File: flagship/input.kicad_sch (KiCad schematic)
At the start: 13 parts, among them J1 BUS_IN, Q1 HOTSWAP_FET, Q2 IDEAL_DIODE_FET, U1 LTC4364IS-1

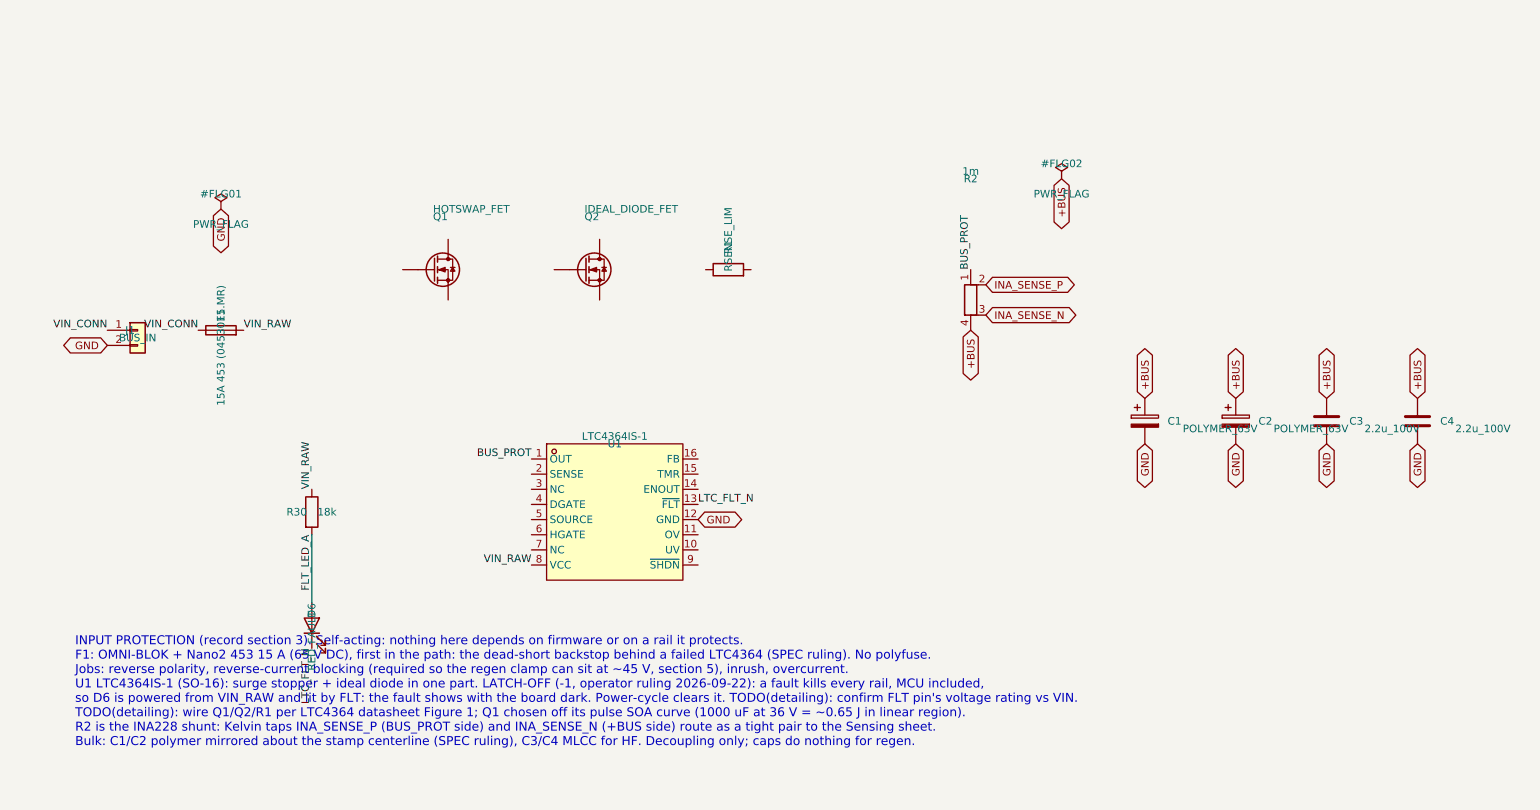
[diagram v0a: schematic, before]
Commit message: flagship: input fuse soldered (Nano2 453 15 A) instead of socketed; SPEC ruling updated
Co-Authored-By: Claude Opus 5.5 (1M context) <noreply@anthropic.com>
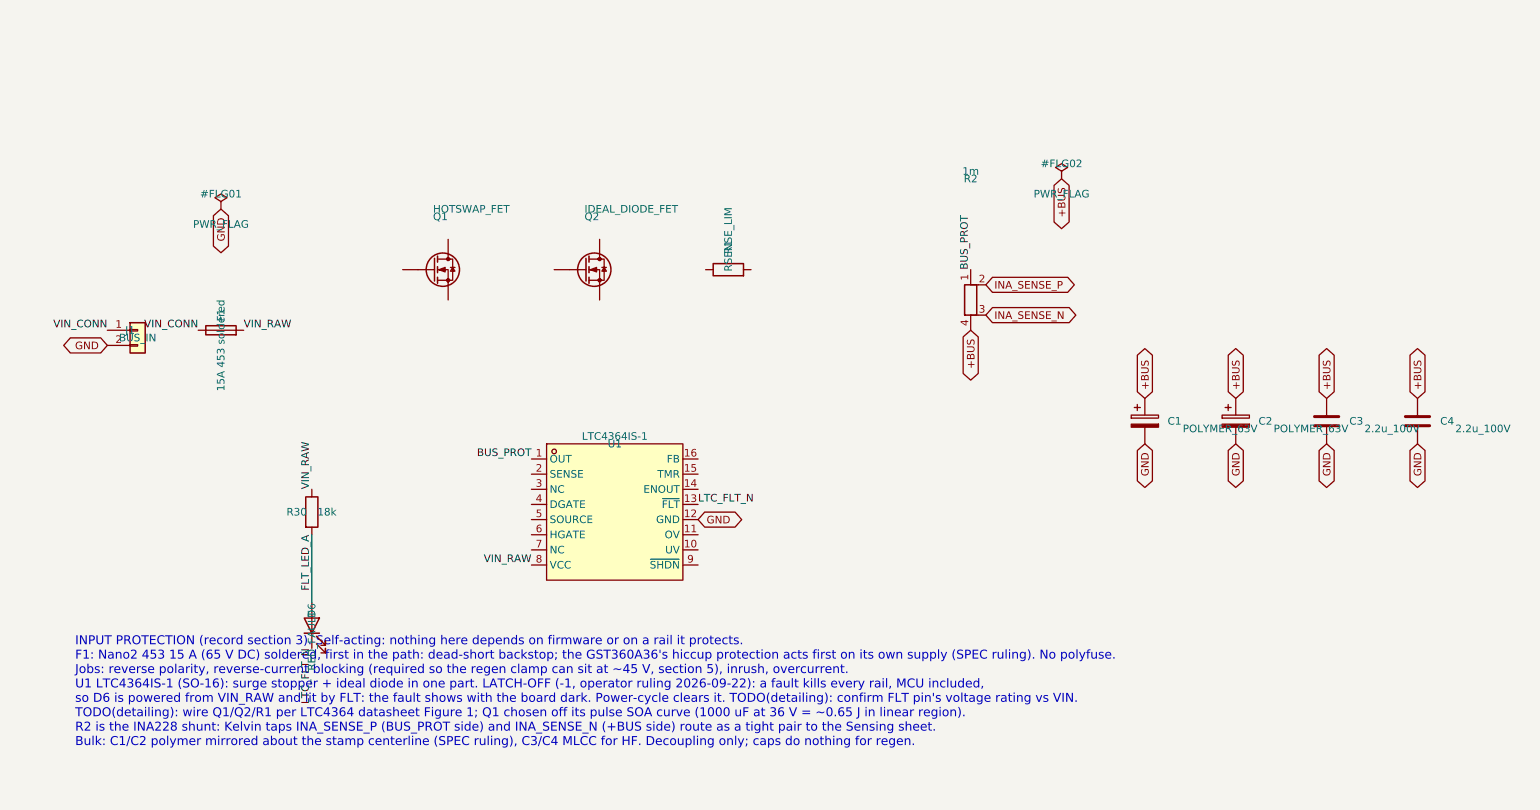
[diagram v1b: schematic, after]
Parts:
- F1: value 15A 453 (0453015.MR) -> 15A 453 soldered; footprint Fuse:Fuseholder_Littelfuse_Nano2_154x -> Fuse:Fuse_Littelfuse-NANO2-451_453
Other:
- note added: "INPUT PROTECTION (record section 3). Self-acting: nothing here depends on firmware or on a rail it protects. F1: Nano2 453 15 A (65 V DC) soldered, first in the path: dead-short backstop; the GST360A36's hiccup protection acts first on its own supply (SPEC ruling). No polyfuse. Jobs: reverse polarity, reverse-current blocking (required so the regen clamp can sit at ~45 V, section 5), inrush, over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"
- note removed: "INPUT PROTECTION (record section 3). Self-acting: nothing here depends on firmware or on a rail it protects. F1: OMNI-BLOK + Nano2 453 15 A (65 V DC), first in the path: the dead-short backstop behind a failed LTC4364 (SPEC ruling). No polyfuse. Jobs: reverse polarity, reverse-current blocking (required so the regen clamp can sit at ~45 V, section 5), inrush, overcurrent. U1 LTC4364IS-1 (SO-16): 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"
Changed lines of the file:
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@@
 	(generator_version "10.0")
 	(paper "A4")
-	(text "INPUT PROTECTION (record section 3). Self-acting: nothing here depends on firmware or on a rail it protects.\nF1: OMNI-BLOK + Nano2 453 15 A (65 V DC), first in the path: the dead-short backstop behind a failed LTC4364 (SPEC ruling). No polyfuse.\nJobs: reverse polarity, reverse-current blocking (required so the regen clamp can sit at ~45 V, section 5), inrush, overcurrent.\nU1 LTC4364IS-1 (SO-16): surge stopper + ideal diode in one part. LATCH-OFF (-1, operator ruling 2026-09-22): a fault kills every rail, MCU included,\nso D6 is powered from VIN_RAW and lit by FLT: the fault shows with the board dark. Power-cycle clears it. TODO(detailing): confirm FLT pin's voltage rating vs VIN.\nTODO(detailing): wire Q1/Q2/R1 per LTC4364 datasheet Figure 1; Q1 chosen off its pulse SOA curve (1000 uF at 36 V = ~0.65 J in linear region).\nR2 is the INA228 shunt: Kelvin taps INA_SENSE_P (BUS_PROT side) and INA_SENSE_N (+BUS side) route as a tight pair to the Sensing sheet.\nBulk: C1/C2 polymer mirrored about the stamp centerline (SPEC ruling), C3/C4 MLCC for HF. Decoupling only; caps do nothing for regen."
+	(text "INPUT PROTECTION (record section 3). Self-acting: nothing here depends on firmware or on a rail it protects.\nF1: Nano2 453 15 A (65 V DC) soldered, first in the path: dead-short backstop; the GST360A36's hiccup protection acts first on its own supply (SPEC ruling). No polyfuse.\nJobs: reverse polarity, reverse-current blocking (required so the regen clamp can sit at ~45 V, section 5), inrush, overcurrent.\nU1 LTC4364IS-1 (SO-16): surge stopper + ideal diode in one part. LATCH-OFF (-1, operator ruling 2026-09-22): a fault kills every rail, MCU included,\nso D6 is powered from VIN_RAW and lit by FLT: the fault shows with the board dark. Power-cycle clears it. TODO(detailing): confirm FLT pin's voltage rating vs VIN.\nTODO(detailing): wire Q1/Q2/R1 per LTC4364 datasheet Figure 1; Q1 chosen off its pulse SOA curve (1000 uF at 36 V = ~0.65 J in linear region).\nR2 is the INA228 shunt: Kelvin taps INA_SENSE_P (BUS_PROT side) and INA_SENSE_N (+BUS side) route as a tight pair to the Sensing sheet.\nBulk: C1/C2 polymer mirrored about the stamp centerline (SPEC ruling), C3/C4 MLCC for HF. Decoupling only; caps do nothing for regen."
 		(exclude_from_sim no)
 		(at 20 150 0)
@@
 			)
 		)
-		(property "Value" "15A 453 (0453015.MR)"
+		(property "Value" "15A 453 soldered"
 			(at 44.45 82.55 0)
 			(show_name no)
@@
 			)
 		)
-		(property "Footprint" "Fuse:Fuseholder_Littelfuse_Nano2_154x"
+		(property "Footprint" "Fuse:Fuse_Littelfuse-NANO2-451_453"
 			(at 44.45 81.788 90)
 			(hide yes)

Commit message: flagship: input protection detailed (LTC4364-1); real FETs and regen resistors picked
Input sheet drawn wired from the LTC4364 datasheet Figure 1 topology: 2.5 mOhm / 20 A
limit, 22 nF HGATE soft ramp, 100 nF timer, 51.5 V output clamp above the regen clamp,
UV 20 V / OV 50 V, 15 V gate zeners, SMBJ45CA bidirectional input TVS, 27k fault LED.
Verified: all input nets exact against the intended table; ERC 0 on the sheet.

Parts: PSMN3R7-100BSE (enhanced-SOA hot-swap D2PAK) in all five power FET positions,
DMN10H220L pre-charge FET, 3x Vishay D2TO35M 24 R regen resistors with isolated tabs to
GND. New project symbols with numbered pins matching the footprints: Q_NMOS_D2PAK
(1 G, 2 D tab, 3 S), Q_NMOS_SOT23 (1 G, 2 S, 3 D), R_D2PAK_TAB (resistor 1/3, tab 2).
Regen sheet regenerated for three resistors; nets exact. Motor CBST raised to 1 uF.
ERC: six of seven sheets at zero errors; Compute awaits GPIO assignment by layout.

Co-Authored-By: Claude Opus 5.5 (1M context) <noreply@anthropic.com>
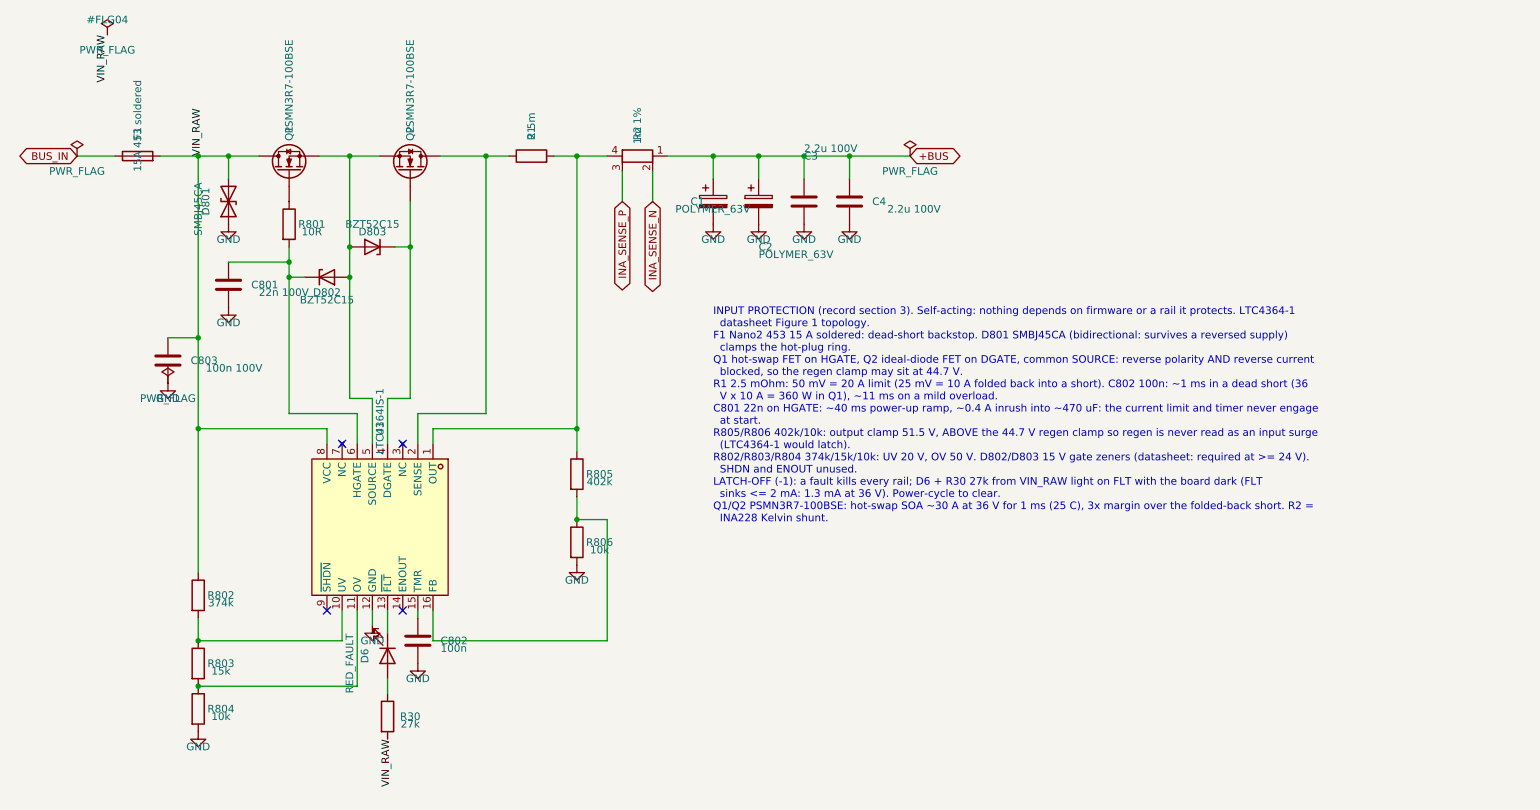
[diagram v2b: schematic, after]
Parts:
- removed J1: BUS_IN, symbol Connector_Generic:Conn_01x02
- removed Q1: HOTSWAP_FET, symbol Device:Q_NMOS
- removed Q2: IDEAL_DIODE_FET, symbol Device:Q_NMOS
- added C801: 22n 100V, Capacitor_SMD:C_0805_2012Metric, symbol Device:C
- added C802: 100n, Capacitor_SMD:C_0805_2012Metric, symbol Device:C
- added C803: 100n 100V, Capacitor_SMD:C_1206_3216Metric, symbol Device:C
- added D801: SMBJ45CA, Diode_SMD:D_SMB, symbol Device:D_TVS
- added D802, D803: BZT52C15, Diode_SMD:D_SOD-123, symbol Device:D_Zener
- added Q1, Q2: PSMN3R7-100BSE, Package_TO_SOT_SMD:TO-263-2, symbol flagship:Q_NMOS_D2PAK
- added R801: 10R, Resistor_SMD:R_0805_2012Metric, symbol Device:R
- added R802: 374k, Resistor_SMD:R_1206_3216Metric, symbol Device:R
- added R803: 15k, Resistor_SMD:R_0805_2012Metric, symbol Device:R
- added R804, R806: 10k, Resistor_SMD:R_0805_2012Metric, symbol Device:R
- added R805: 402k, Resistor_SMD:R_1206_3216Metric, symbol Device:R
- C3, C4: value 2.2u_100V -> 2.2u 100V
- R1: value RSENSE_LIM -> 2.5m
- R2: value 1m -> 1m 1%; footprint (none) -> Resistor_SMD:R_Shunt_Vishay_WSK2512_6332Metric_T1.19mm
- R30: value 18k -> 27k
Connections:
- net +BUS: now also R2.1; no longer R2.4
- net GND: now also C801.2, C802.2, C803.2, D801.1 (A1), R804.2, R806.2
- net INA_SENSE_N: now also R2.2; no longer R2.3
- net INA_SENSE_P: now also R2.3; no longer R2.2
- net VIN_RAW: now also R30.2, C803.1, D801.2 (A2), Q1.2 (D), R802.1; no longer R30.1
- net at R1.1: now also U1.2 (SENSE), Q2.2 (D)
- net at R1.2: now also R2.4, U1.1 (OUT), R805.1
- net at U1.10 (UV): now also R802.2, R803.1
- net at U1.11 (OV): now also R803.2, R804.1
- net at U1.15 (TMR): now also C802.1
- net at U1.16 (FB): now also R805.2, R806.1
- net at U1.4 (DGATE): now also D803.1 (K), Q2.1 (G)
- net at U1.5 (SOURCE): now also D802.2 (A), D803.2 (A), Q1.3 (S), Q2.3 (S)
- net at U1.6 (HGATE): now also C801.1, D802.1 (K), R801.2
- removed net BUS_PROT: R2.1, U1.1 (OUT)
- net FLT_LED_A: no longer names the net of D6.2 (A)
- net FLT_LED_A: now also R30.1; no longer R30.2
- net LTC_FLT_N: no longer names the net of D6.1 (K), U1.13 (~{FLT})
- net VIN_CONN renamed BUS_IN
- new net: Q1.1 (G), R801.1
- no-connect marks 0 -> 4
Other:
- note added: "INPUT PROTECTION (record section 3). Self-acting: nothing depends on firmware or a rail it protects. LTC4364-1 datasheet Figure 1 topology. F1 Nano2 453 15 A soldered: dead-short backstop. D801 SMBJ45CA (bidirectional: survives a reversed supply) clamps the hot-plug ring. Q1 hot-swap FET on HGATE, Q2 ideal-diode FET on DGATE, common SOURCE: reverse polarity AND reverse current blocked, so the reg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"
- note removed: "INPUT PROTECTION (record section 3). Self-acting: nothing here depends on firmware or on a rail it protects. F1: Nano2 453 15 A (65 V DC) soldered, first in the path: dead-short backstop; the GST360A36's hiccup protection acts first on its own supply (SPEC ruling). No polyfuse. Jobs: reverse polarity, reverse-current blocking (required so the regen clamp can sit at ~45 V, section 5), inrush, over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"

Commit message: flagship: Kelvin WSK2512 shunts everywhere (LTC4364 sense now 4-terminal), bulk and MLCC parts picked
R1 (LTC4364, 2.5 mOhm) becomes a 4-terminal shunt with SENSE and OUT on its Kelvin taps;
R1/R2/R401 all Vishay WSK2512 on the T2.21 mm footprint that value range needs. Bulk:
2x EEH-ZA1J101P 100 uF 63 V hybrid polymer + 2x GRM32ER72A225KA35L; buck input caps get
the same MLCC part number. Regen resistors labeled D2TO35M 24 R 2 %. Input nets verified
exact after regeneration; ERC 0 on every detailed sheet.

Co-Authored-By: Claude Opus 5.5 (1M context) <noreply@anthropic.com>
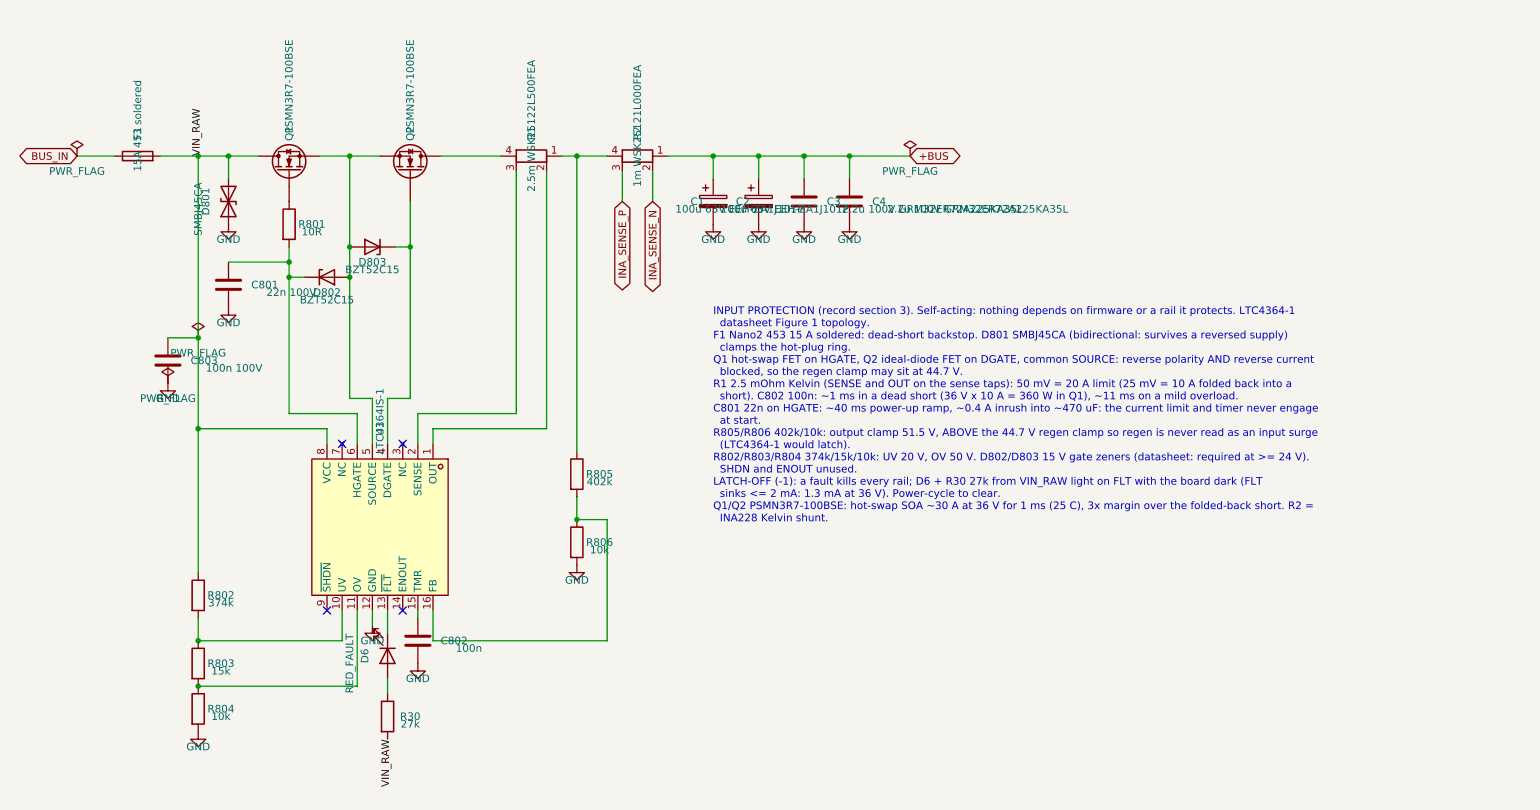
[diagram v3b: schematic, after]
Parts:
- removed R1: 2.5m, Resistor_SMD:R_2512_6332Metric, symbol Device:R
- added R1: 2.5m WSK25122L500FEA, Resistor_SMD:R_Shunt_Vishay_WSK2512_6332Metric_T2.21mm, symbol Device:R_Shunt
- C1, C2: value POLYMER_63V -> 100u 63V EEH-ZA1J101P; footprint (none) -> Capacitor_SMD:CP_Elec_10x10.5
- C3, C4: value 2.2u 100V -> 2.2u 100V GRM32ER72A225KA35L
- R2: value 1m 1% -> 1m WSK25121L000FEA; footprint Resistor_SMD:R_Shunt_Vishay_WSK2512_6332Metric_T1.19mm -> Resistor_SMD:R_Shunt_Vishay_WSK2512_6332Metric_T2.21mm
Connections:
- net at R2.4, R805.1: now also R1.1; no longer U1.1 (OUT)
- net at Q2.2 (D): now also R1.4; no longer U1.2 (SENSE)
- new net: R1.2, U1.1 (OUT)
- new net: R1.3, U1.2 (SENSE)
